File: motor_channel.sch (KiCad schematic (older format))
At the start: 19 parts

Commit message: Motor capacitors, test points, jumpers
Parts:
- C? (x4): value C -> 100n
- C? (x2): value C -> 10n
- R? (x2): value 1k -> 220
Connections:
- net labels added: pwm1, pwm2
- net labels removed: APWM, BPWM
- wire segments 52 -> 51
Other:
- moved on the sheet: C?, D?, R?

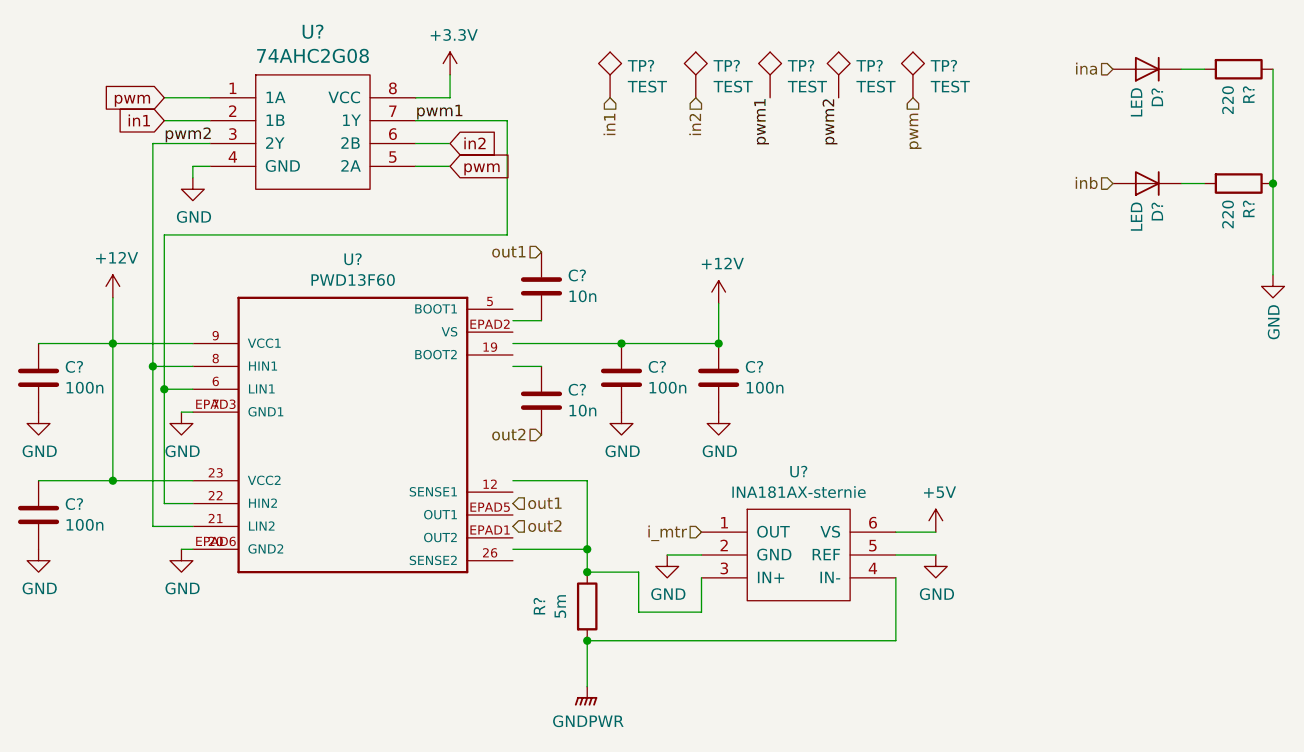
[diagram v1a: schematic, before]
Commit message: Eletrical Rules Check
Fixed some label names
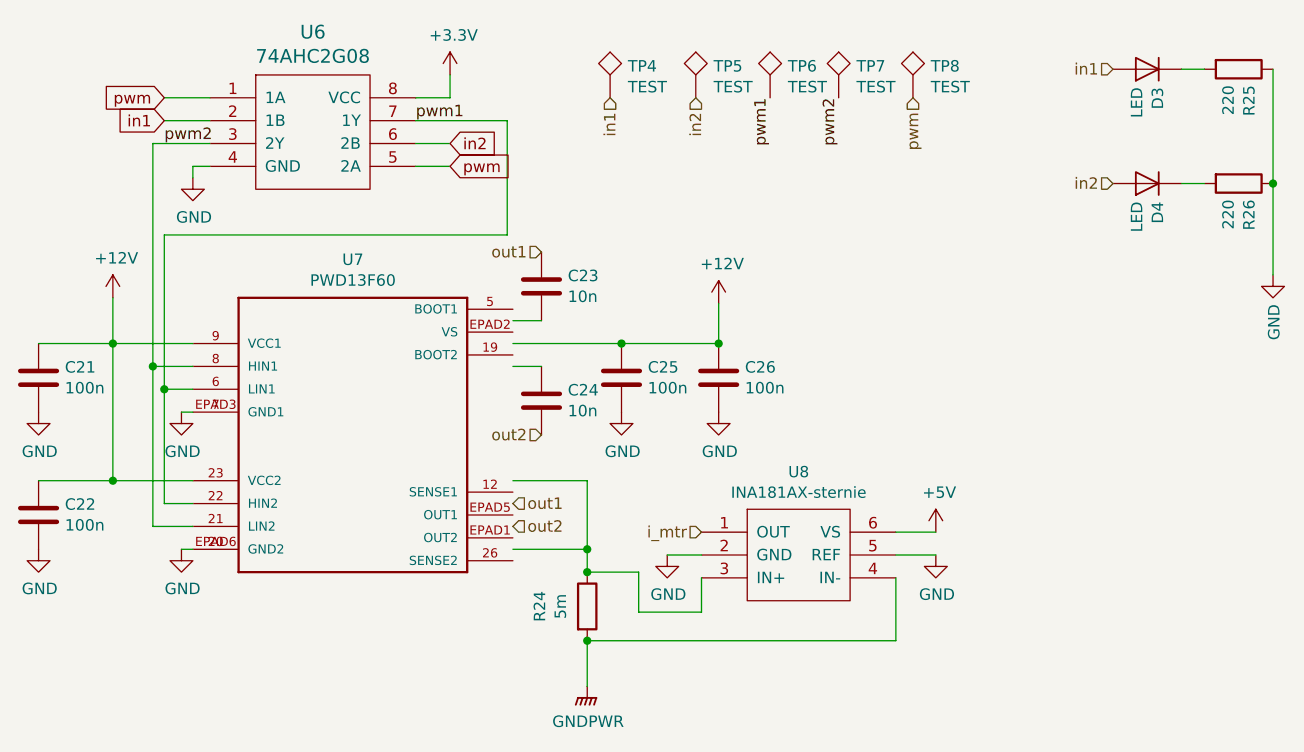
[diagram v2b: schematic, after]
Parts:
- gave numbers to parts that had none: 19
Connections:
- net labels removed: ina, inb

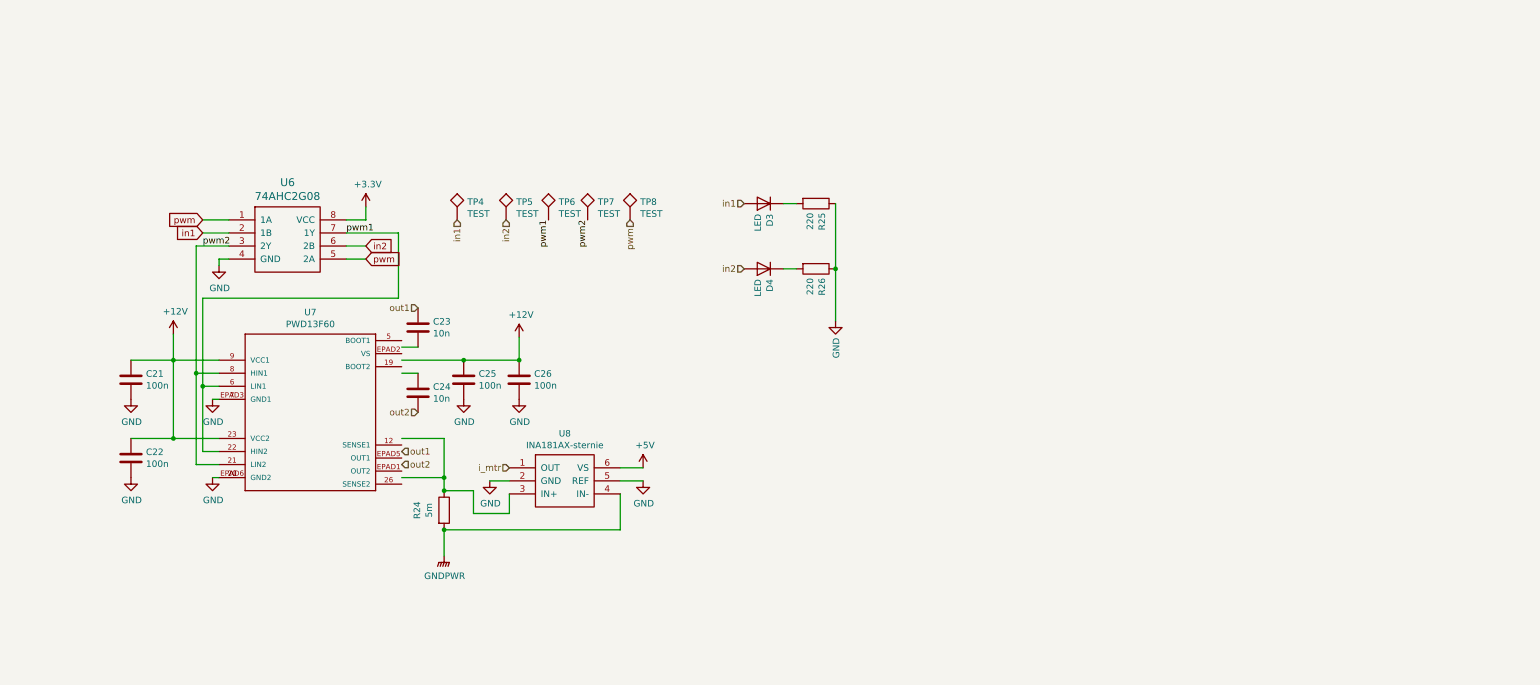
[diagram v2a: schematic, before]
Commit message: Formatting Changes
Made some minor formatting changes. Documented motor channels. Fixed in labels of motor channel.
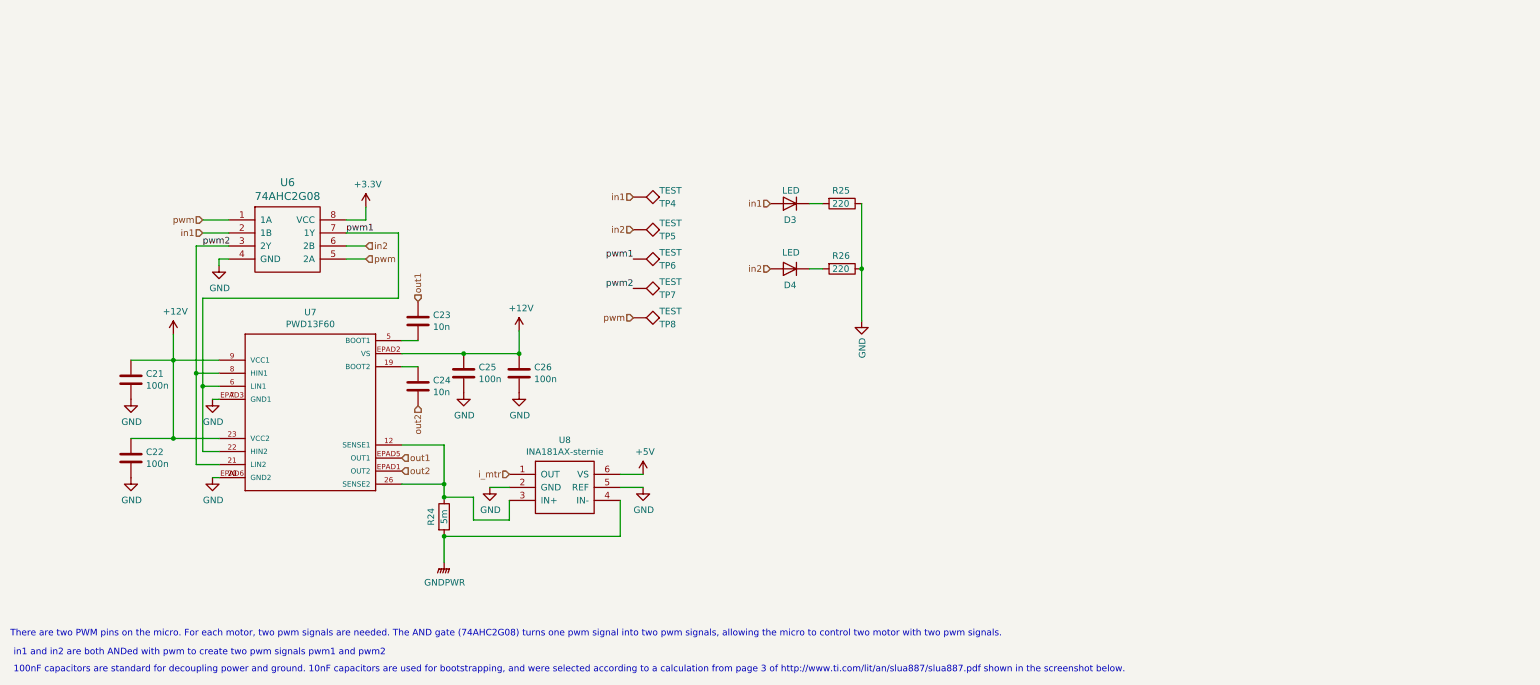
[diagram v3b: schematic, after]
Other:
- note added: "100nF capacitors are standard for decoupling power and ground. 10nF capacitors are used for bootstrapping, and were selected according to a calculation from page 3 of http://www.ti.com/lit/an/slua887/slua887.pdf shown in the screenshot below.\n"
- note added: "There are two PWM pins on the micro. For each motor, two pwm signals are needed. The AND gate (74AHC2G08) turns one pwm signal into two pwm signals, allowing the micro to control two motor with two pwm signals."
- note added: "in1 and in2 are both ANDed with pwm to create two pwm signals pwm1 and pwm2\n\n"
- moved on the sheet: C23, C24, C25, C26, D3, D4, R24, R25, R26, TP4, U8

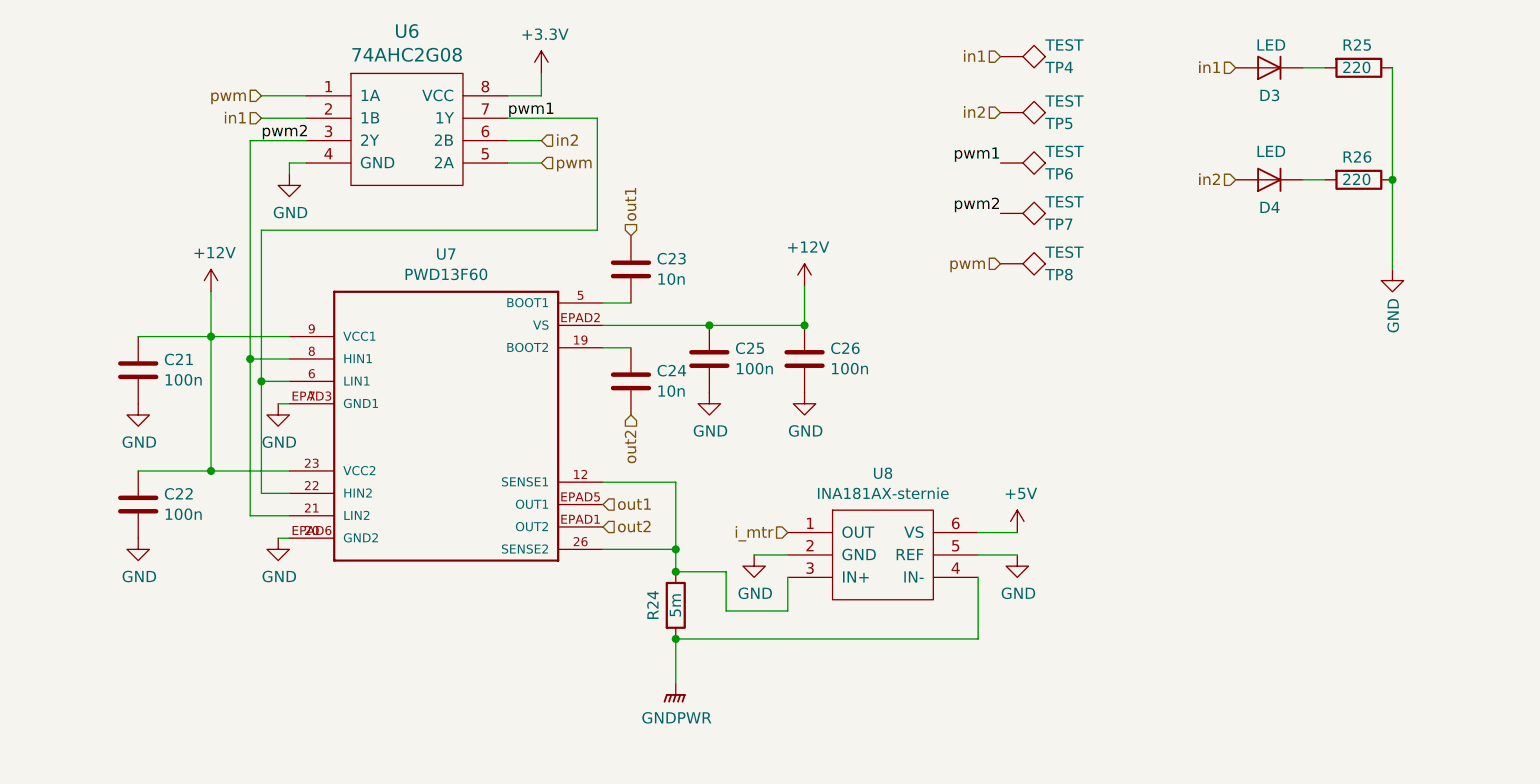
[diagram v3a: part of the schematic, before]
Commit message: renamed motor controller input name and moved adc pinouts
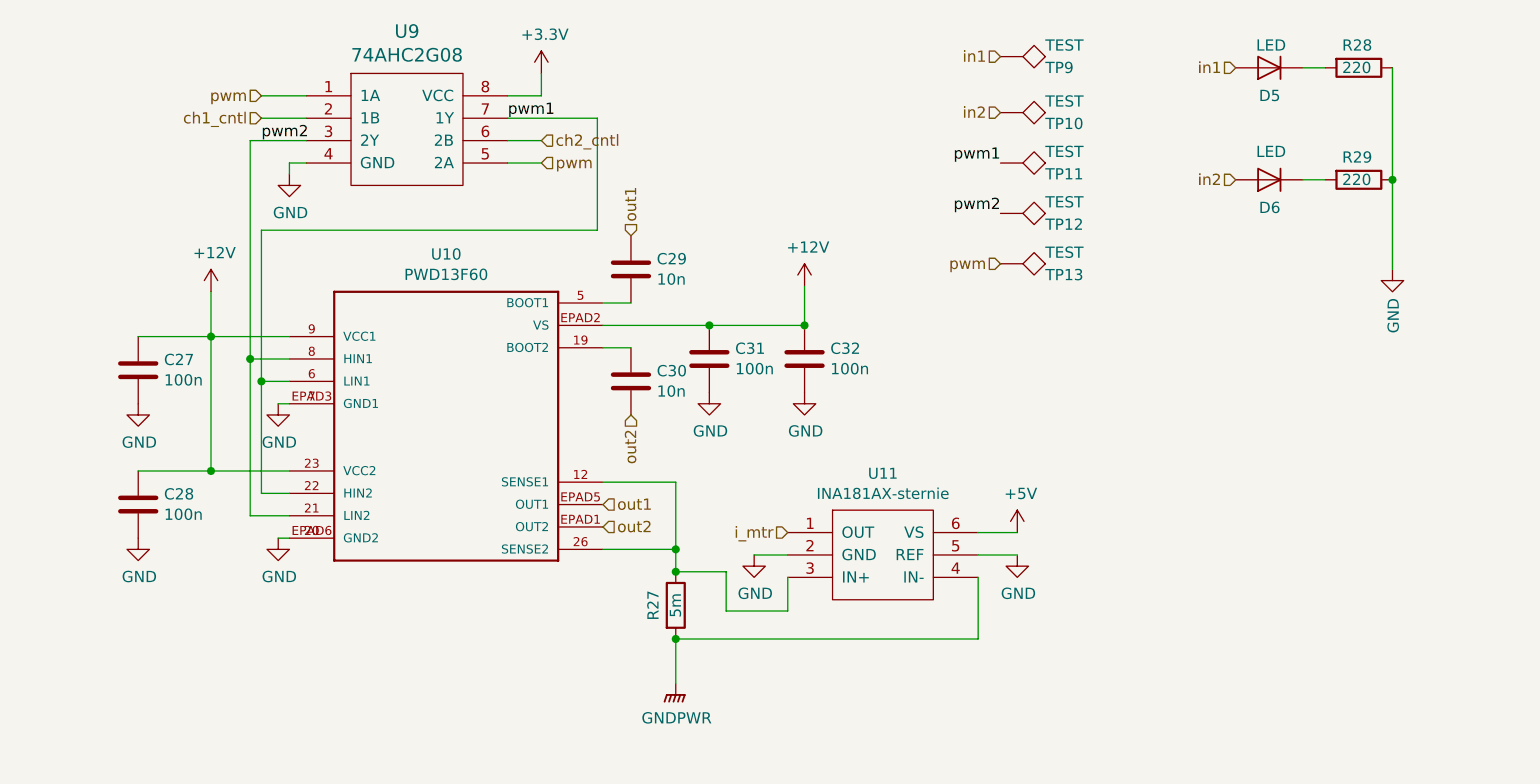
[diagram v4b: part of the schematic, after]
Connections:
- net in1: no longer U6.2 (1B)
- net in2: no longer U6.6 (2B)
- new net ch1_cntl: U6.2 (1B)
- new net ch2_cntl: U6.6 (2B)
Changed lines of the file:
@@
 $Descr A4 11693 8268
 encoding utf-8
-Sheet 7 12
+Sheet 8 12
 Title ""
 Date ""
@@
 AR Path="/5E49EA18/5E6AD26A/5E507B4D" Ref="U?"  Part="1"
 AR Path="/5E49EA18/5E6EF1BC/5E507B4D" Ref="U10"  Part="1"
-F 0 "U7" H 3625 4892 50  0000 C CNN
+F 0 "U10" H 3625 4892 50  0000 C CNN
 F 1 "PWD13F60" H 3625 4801 50  0000 C CNN
 F 2 "CONV_PWD13F60" H 3625 4125 50  0001 L BNN
@@
 AR Path="/5E49EA18/5E6AD26A/5E6371F6" Ref="R?"  Part="1"
 AR Path="/5E49EA18/5E6EF1BC/5E6371F6" Ref="R27"  Part="1"
-F 0 "R24" V 4550 4925 50  0000 C CNN
+F 0 "R27" V 4550 4925 50  0000 C CNN
 F 1 "5m" V 4650 4925 50  0000 C CNN
 F 2 "" V 4580 4925 50  0001 C CNN
@@
 AR Path="/5E49EA18/5E6AD26A/5E634929" Ref="U?"  Part="1"
 AR Path="/5E49EA18/5E6EF1BC/5E634929" Ref="U11"  Part="1"
-F 0 "U8" H 5575 5063 49  0000 C CNN
+F 0 "U11" H 5575 5063 49  0000 C CNN
 F 1 "INA181AX-sternie" H 5575 4973 49  0000 C CNN
 F 2 "" H 5150 5000 49  0001 C CNN
@@
 AR Path="/5E49EA18/5E507A5C/5E66FBCB" Ref="D3"  Part="1"
 AR Path="/5E49EA18/5E6EF1BC/5E66FBCB" Ref="D5"  Part="1"
-F 0 "D3" H 7250 2650 50  0000 L CNN
+F 0 "D5" H 7250 2650 50  0000 L CNN
 F 1 "LED" H 7225 2425 50  0000 L CNN
 F 2 "" H 7300 2525 50  0001 C CNN
@@
 AR Path="/5E49EA18/5E507A5C/5E6708D8" Ref="D4"  Part="1"
 AR Path="/5E49EA18/5E6EF1BC/5E6708D8" Ref="D6"  Part="1"
-F 0 "D4" H 7250 3150 50  0000 L CNN
+F 0 "D6" H 7250 3150 50  0000 L CNN
 F 1 "LED" H 7225 2900 50  0000 L CNN
 F 2 "" H 7300 3025 50  0001 C CNN
@@
 AR Path="/5E49EA18/5E507A5C/5E67277D" Ref="R25"  Part="1"
 AR Path="/5E49EA18/5E6EF1BC/5E67277D" Ref="R28"  Part="1"
-F 0 "R25" V 7600 2450 50  0000 L CNN
+F 0 "R28" V 7600 2450 50  0000 L CNN
 F 1 "220" V 7700 2450 50  0000 L CNN
 F 2 "" V 7630 2525 50  0001 C CNN
@@
 AR Path="/5E49EA18/5E507A5C/5E673457" Ref="R26"  Part="1"
 AR Path="/5E49EA18/5E6EF1BC/5E673457" Ref="R29"  Part="1"
-F 0 "R26" V 7600 2950 50  0000 L CNN
+F 0 "R29" V 7600 2950 50  0000 L CNN
 F 1 "220" V 7700 2950 50  0000 L CNN
 F 2 "" V 7630 3025 50  0001 C CNN
@@
 AR Path="/5E49EA18/5E507A5C/5E659488" Ref="U6"  Part="1"
 AR Path="/5E49EA18/5E6EF1BC/5E659488" Ref="U9"  Part="1"
-F 0 "U6" H 3450 2337 60  0000 C CNN
+F 0 "U9" H 3450 2337 60  0000 C CNN
 F 1 "74AHC2G08" H 3450 2231 60  0000 C CNN
 F 2 "" H 3000 2350 60  0001 C CNN
@@
 AR Path="/5E49EA18/5E507A5C/5E6CD1E7" Ref="C25"  Part="1"
 AR Path="/5E49EA18/5E6EF1BC/5E6CD1E7" Ref="C31"  Part="1"
-F 0 "C25" H 4915 3871 50  0000 L CNN
+F 0 "C31" H 4915 3871 50  0000 L CNN
 F 1 "100n" H 4915 3780 50  0000 L CNN
 F 2 "" H 4838 3675 50  0001 C CNN
@@
 AR Path="/5E49EA18/5E507A5C/5E6CE986" Ref="C26"  Part="1"
 AR Path="/5E49EA18/5E6EF1BC/5E6CE986" Ref="C32"  Part="1"
-F 0 "C26" H 5340 3871 50  0000 L CNN
+F 0 "C32" H 5340 3871 50  0000 L CNN
 F 1 "100n" H 5340 3780 50  0000 L CNN
 F 2 "" H 5263 3675 50  0001 C CNN
@@
 AR Path="/5E49EA18/5E507A5C/5E6C3B2F" Ref="C21"  Part="1"
 AR Path="/5E49EA18/5E6EF1BC/5E6C3B2F" Ref="C27"  Part="1"
-F 0 "C21" H 2365 3921 50  0000 L CNN
+F 0 "C27" H 2365 3921 50  0000 L CNN
 F 1 "100n" H 2365 3830 50  0000 L CNN
 F 2 "" H 2288 3725 50  0001 C CNN
@@
 AR Path="/5E49EA18/5E507A5C/5E6C48A1" Ref="C22"  Part="1"
 AR Path="/5E49EA18/5E6EF1BC/5E6C48A1" Ref="C28"  Part="1"
-F 0 "C22" H 2365 4521 50  0000 L CNN
+F 0 "C28" H 2365 4521 50  0000 L CNN
 F 1 "100n" H 2365 4430 50  0000 L CNN
 F 2 "" H 2288 4325 50  0001 C CNN
@@
 AR Path="/5E49EA18/5E507A5C/5E6C896D" Ref="C24"  Part="1"
 AR Path="/5E49EA18/5E6EF1BC/5E6C896D" Ref="C30"  Part="1"
-F 0 "C24" H 4565 3971 50  0000 L CNN
+F 0 "C30" H 4565 3971 50  0000 L CNN
 F 1 "10n" H 4565 3880 50  0000 L CNN
 F 2 "" H 4488 3775 50  0001 C CNN
@@
 AR Path="/5E49EA18/5E507A5C/5E6C6CA0" Ref="C23"  Part="1"
 AR Path="/5E49EA18/5E6EF1BC/5E6C6CA0" Ref="C29"  Part="1"
-F 0 "C23" H 4565 3471 50  0000 L CNN
+F 0 "C29" H 4565 3471 50  0000 L CNN
 F 1 "10n" H 4565 3380 50  0000 L CNN
 F 2 "" H 4488 3275 50  0001 C CNN
@@
 $EndBitmap
 Text HLabel 2800 2750 0    50   Input ~ 0
-in1
+ch1_cntl
 Text HLabel 4050 2850 2    50   Input ~ 0
-in2
+ch2_cntl
 Text Notes 1350 6075 0    50   ~ 0
 in1 and in2 are both ANDed with pwm to create two pwm signals pwm1 and pwm2\n\n
@@
 AR Path="/5E49EA18/5E507A5C/5E66AC4A" Ref="TP4"  Part="1"
 AR Path="/5E49EA18/5E6EF1BC/5E66AC4A" Ref="TP9"  Part="1"
-F 0 "TP4" V 6150 2675 50  0000 L CNN
+F 0 "TP9" V 6150 2675 50  0000 L CNN
 F 1 "TEST" V 6050 2675 50  0000 L CNN
 F 2 "" H 6100 2475 50  0001 C CNN
@@
 AR Path="/5E49EA18/5E507A5C/5E7B8563" Ref="TP5"  Part="1"
 AR Path="/5E49EA18/5E6EF1BC/5E7B8563" Ref="TP10"  Part="1"
-F 0 "TP5" V 6150 2925 50  0000 L CNN
+F 0 "TP10" V 6150 2925 50  0000 L CNN
 F 1 "TEST" V 6050 2925 50  0000 L CNN
 F 2 "" H 6100 2725 50  0001 C CNN
@@
 AR Path="/5E49EA18/5E507A5C/5E7B95BB" Ref="TP6"  Part="1"
 AR Path="/5E49EA18/5E6EF1BC/5E7B95BB" Ref="TP11"  Part="1"
-F 0 "TP6" V 6150 3150 50  0000 L CNN
+F 0 "TP11" V 6150 3150 50  0000 L CNN
 F 1 "TEST" V 6050 3150 50  0000 L CNN
 F 2 "" H 6100 2950 50  0001 C CNN
@@
 AR Path="/5E49EA18/5E507A5C/5E7BA52F" Ref="TP7"  Part="1"
 AR Path="/5E49EA18/5E6EF1BC/5E7BA52F" Ref="TP12"  Part="1"
-F 0 "TP7" V 6150 3375 50  0000 L CNN
+F 0 "TP12" V 6150 3375 50  0000 L CNN
 F 1 "TEST" V 6050 3375 50  0000 L CNN
 F 2 "" H 6100 3175 50  0001 C CNN
@@
 AR Path="/5E49EA18/5E507A5C/5E7BB59A" Ref="TP8"  Part="1"
 AR Path="/5E49EA18/5E6EF1BC/5E7BB59A" Ref="TP13"  Part="1"
-F 0 "TP8" V 6150 3600 50  0000 L CNN
+F 0 "TP13" V 6150 3600 50  0000 L CNN
 F 1 "TEST" V 6050 3600 50  0000 L CNN
 F 2 "" H 6100 3400 50  0001 C CNN

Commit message: fixed up pwm control to hbridge
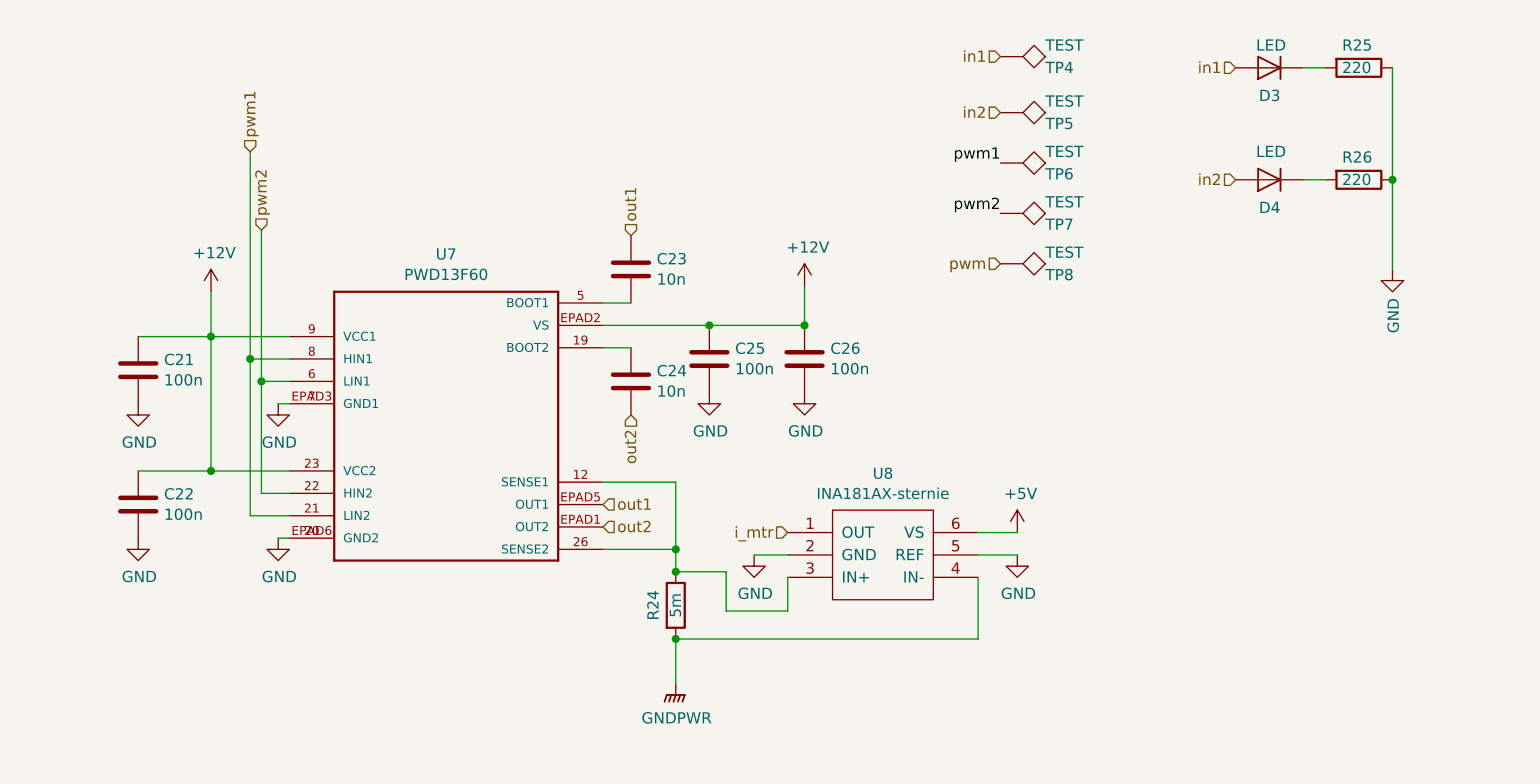
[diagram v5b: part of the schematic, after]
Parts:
- removed U6: 74AHC2G08, symbol ec_2b_rescue:74AHC2G08
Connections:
- net pwm1: now also U7.21 (LIN2), U7.8 (HIN1); no longer U7.22 (HIN2), U7.6 (LIN1)
- net pwm2: now also U7.22 (HIN2), U7.6 (LIN1); no longer U7.21 (LIN2), U7.8 (HIN1)
